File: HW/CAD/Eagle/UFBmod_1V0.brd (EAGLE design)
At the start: 78.1 x 89.8 mm, 63 parts, among them U101 DIGILENT_CMOD_A7, U301 MAX5217, U401 AT86RF215-ZU, U411 ASVTX-13-D-26.000MHZ-I05-T, U511 PE4259, U581 B39871B3440U410, U611 TPS62056DGSR, X599 ANTENNATINY

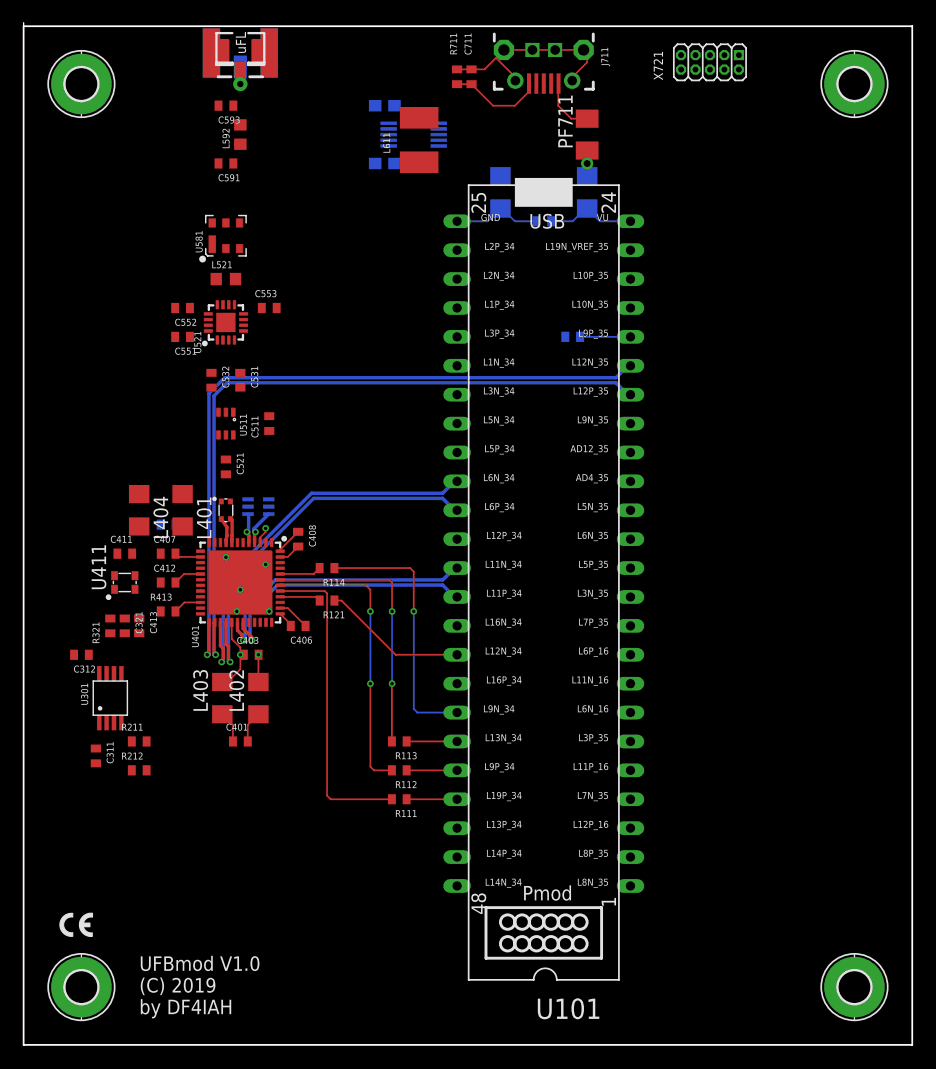
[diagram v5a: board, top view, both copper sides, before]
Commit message: HW_1V0 - CAD/Eagle - connectors added
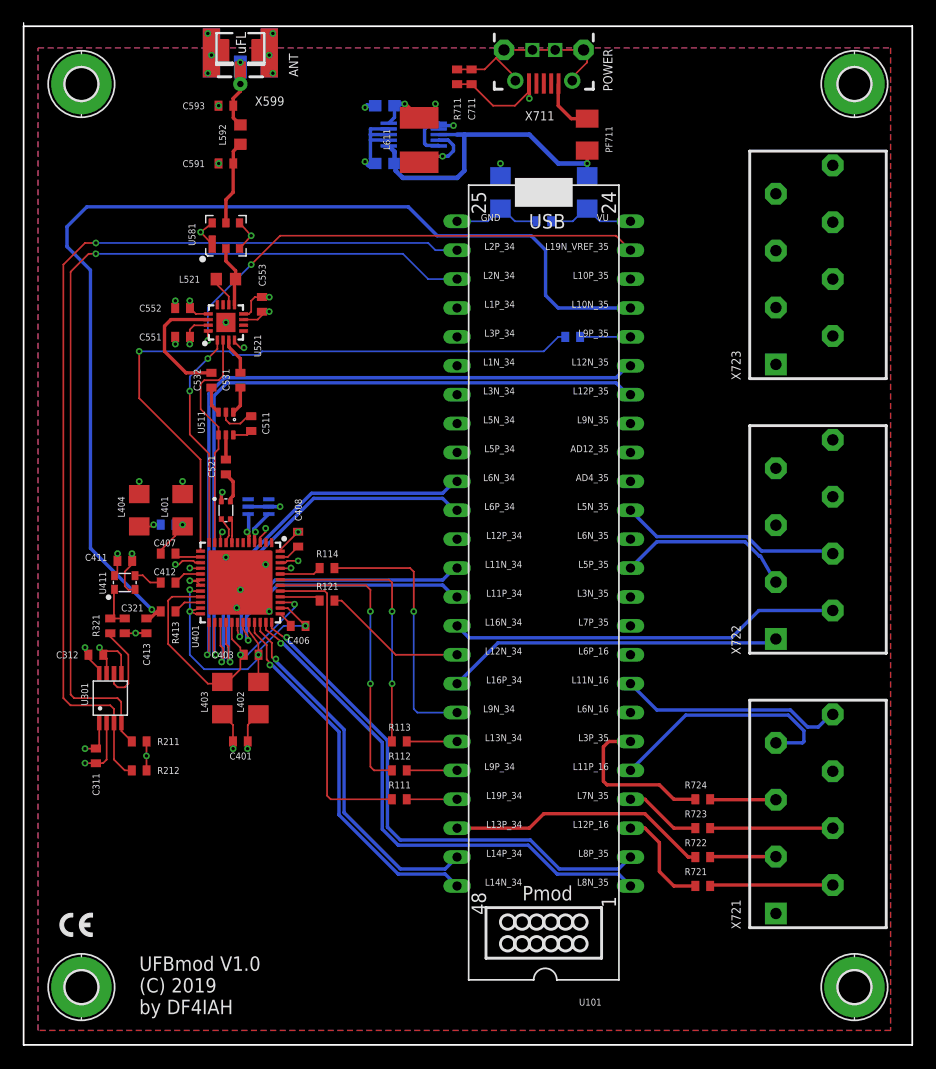
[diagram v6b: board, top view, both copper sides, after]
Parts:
- added R721, R722, R723, R724: 100R, df4iah_rcl:R0402
- added X722, X723: PHOENIX_1990067_1X8X2MM50_PTSA-0-5, df4iah_connector:PHOENIX_1990067_1X8X2MM50_PTSA-0-5
- X721: value (none) -> PHOENIX_1990067_1X8X2MM50_PTSA-0-5; device df4iah_connector:2X05_1MM27 -> df4iah_connector:PHOENIX_1990067_1X8X2MM50_PTSA-0-5
- moved X721 68.2 mm to (71.1, 19.1), turned to 90 degrees
- moved C511 1.59 mm to (20.0, 54.6)
- moved C312 1.27 mm to (6.35, 34.3)
- moved C553 0.71 mm to (21.0, 65.1), turned to 90 degrees
- moved C413 0.63 mm to (10.8, 36.8)
- moved C411 0.63 mm to (8.89, 42.5)
- renumbered J711 to X711
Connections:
- new net FPGA_11_16_N: U101.8, X721.8
- new net FPGA_11_16_P: U101.5, X721.7
- new net FPGA_12P16: R721.1, U101.3
- new net FPGA_12P16_R: R721.2, X721.2
- new net FPGA_13P_34: R722.1, U101.46
- new net FPGA_13P_34_R: R722.2, X721.3
- new net FPGA_16_34_N: U101.39, X722.2
- new net FPGA_16_34_P: U101.41, X722.1
- new net FPGA_3P35: R724.1, U101.6
- new net FPGA_3P35_R: R724.2, X721.5
- new net FPGA_3_34_N: U101.29
- new net FPGA_3_34_P: U101.31
- new net FPGA_5_34_N: U101.32, X722.6
- new net FPGA_5_34_P: U101.33, X722.5
- new net FPGA_5_35_N: U101.14, X722.4
- new net FPGA_5_35_P: U101.12, X722.3
- new net FPGA_7N35: R723.1, U101.4
- new net FPGA_7N35_R: R723.2, X721.4
- net GND: now also X721.1, X721.6
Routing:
- net FPGA_TRX_CLKO: track 0.00 -> 95.0 mm, vias 0 -> 1
- net FPGA_I2C_SCL: track 0.00 -> 85.0 mm, vias 0 -> 1
- net FPGA_I2C_SDA: track 0.00 -> 81.3 mm, vias 0 -> 1
- net GND: track 11.1 -> 72.3 mm, vias 0 -> 29
- net TRX_RSTN: track 0.00 -> 58.0 mm, vias 0 -> 1
- net TRX_RXD24_N: track 0.00 -> 46.7 mm, vias 0 -> 1
- net TRX_RXD24_P: track 0.00 -> 45.9 mm, vias 0 -> 1
- net FE09_MODE: track 0.00 -> 44.0 mm, vias 0 -> 2
- net FPGA_16_34_N: track 0.00 -> 34.4 mm
- net TRX_RXCLK_N: track 0.00 -> 33.3 mm, vias 0 -> 1
- net TRX_RXCLK_P: track 0.00 -> 32.5 mm, vias 0 -> 1
- net +3V3: track 2.78 -> 34.9 mm, vias 0 -> 11
- net FPGA_16_34_P: track 0.00 -> 29.6 mm
- net +5V: track 2.26 -> 28.5 mm
- net TRX_DVSS: track 5.28 -> 29.7 mm, vias 1 -> 4
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- added copper zone on layer 15, net +3V3
- added copper zone on layer 1, net GND
- added copper zone on layer 16, net GND
- added copper zone on layer 2, net GND
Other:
- board text added: "ANT"
- board text added: "POWER"
- board text added: "X599"

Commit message: HW_1V0 - CAD/Eagle - one more line pair added to the connector
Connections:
- net FPGA_3_34_N: now also X722.8
- net FPGA_3_34_P: now also X722.7
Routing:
- net FPGA_3_34_N: track 0.00 -> 36.8 mm
- net FPGA_5_34_N: track 0.00 -> 35.7 mm
- net FPGA_3_34_P: track 0.00 -> 33.3 mm
- net FPGA_5_34_P: track 0.00 -> 32.1 mm
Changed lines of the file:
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@@
 <contactref element="X722" pad="5"/>
 <contactref element="U101" pad="33"/>
-<wire x1="38.1" y1="52.07" x2="66.12" y2="45.68" width="0" layer="19" extent="1-1"/>
+<wire x1="38.1" y1="52.07" x2="38.325" y2="52.07" width="0.3" layer="16"/>
+<wire x1="38.325" y1="52.07" x2="39.37" y2="53.115" width="0.3" layer="16"/>
+<wire x1="39.37" y1="53.115" x2="43.0868" y2="53.115" width="0.3" layer="16"/>
+<wire x1="43.0868" y1="53.115" x2="48.1668" y2="48.035" width="0.3" layer="16"/>
+<wire x1="48.1668" y1="48.035" x2="64.77" y2="48.035" width="0.3" layer="16"/>
+<wire x1="64.77" y1="48.035" x2="66.12" y2="46.685" width="0.3" layer="16"/>
+<wire x1="66.12" y1="46.685" x2="66.12" y2="45.68" width="0.3" layer="16"/>
 </signal>
 <signal name="FPGA_5_34_N" class="1">
 <contactref element="X722" pad="6"/>
 <contactref element="U101" pad="32"/>
-<wire x1="38.1" y1="54.61" x2="71.12" y2="48.18" width="0" layer="19" extent="1-1"/>
+<wire x1="38.1" y1="54.61" x2="38.325" y2="54.61" width="0.3" layer="16"/>
+<wire x1="38.325" y1="54.61" x2="39.37" y2="53.565" width="0.3" layer="16"/>
+<wire x1="39.37" y1="53.565" x2="43.2732" y2="53.565" width="0.3" layer="16"/>
+<wire x1="43.2732" y1="53.565" x2="48.3532" y2="48.485" width="0.3" layer="16"/>
+<wire x1="48.3532" y1="48.485" x2="70.815" y2="48.485" width="0.3" layer="16"/>
+<wire x1="70.815" y1="48.485" x2="71.12" y2="48.18" width="0.3" layer="16"/>
 </signal>
 <signal name="FPGA_3_34_P" class="1">
 <contactref element="U101" pad="31"/>
+<contactref element="X722" pad="7"/>
+<wire x1="38.1" y1="57.15" x2="40.415" y2="59.465" width="0.3" layer="1"/>
+<wire x1="40.415" y1="59.465" x2="44.3568" y2="59.465" width="0.3" layer="1"/>
+<wire x1="44.3568" y1="59.465" x2="50.7068" y2="53.115" width="0.3" layer="1"/>
+<wire x1="50.7068" y1="53.115" x2="64.77" y2="53.115" width="0.3" layer="1"/>
+<wire x1="64.77" y1="53.115" x2="66.12" y2="51.765" width="0.3" layer="1"/>
+<wire x1="66.12" y1="51.765" x2="66.12" y2="50.68" width="0.3" layer="1"/>
 </signal>
 <signal name="FPGA_3_34_N" class="1">
 <contactref element="U101" pad="29"/>
+<contactref element="X722" pad="8"/>
+<wire x1="38.1" y1="62.23" x2="40.415" y2="59.915" width="0.3" layer="1"/>
+<wire x1="40.415" y1="59.915" x2="44.5432" y2="59.915" width="0.3" layer="1"/>
+<wire x1="44.5432" y1="59.915" x2="50.8932" y2="53.565" width="0.3" layer="1"/>
+<wire x1="50.8932" y1="53.565" x2="70.735" y2="53.565" width="0.3" layer="1"/>
+<wire x1="70.735" y1="53.565" x2="71.12" y2="53.18" width="0.3" layer="1"/>
 </signal>
 </signals>

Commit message: HW_1V0 - V1.0 at the board house
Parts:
- added C221, C222: 1nF, df4iah_rcl:C0402
- added C595, C597: 0pF, df4iah_rcl:C0402
- added D141: ASMT-YTB7-0AA02_RGB, df4iah_led:ASMT-YTB7_0AA02_RGB
- added FIDU_BL, FIDU_BR, FIDU_TL, FIDU_TR: (no value), df4iah_fiducial:FIDUCIAL_MARK_1MM
- added L596: 0nH, df4iah_rcl:L0603
- added R141: 180R, df4iah_rcl:R0402
- added R142, R143: 130R, df4iah_rcl:R0402
- added R151, R152, R521: 1kR, df4iah_rcl:R0402
- added R733, R734, R735, R736: 100R, df4iah_rcl:R0402
- added X221: TTE_EN11-HSM, df4iah_switch:TTE_EN11-HSM
- added X595: ANTENNATINY, _c2h:SMA_UFL_PAD_TINY
- U521: value (none) -> RFX1010
- X711: value (none) -> MOLEX 105017-0001
- renumbered X599 to X591
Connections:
- net ANT renamed ANT09
- net ANT_MATCH renamed ANT09_MATCH
- new net ANT24: C597.1, L596.2, X595.ANT1, X595.ANT2, X595.ANT3
- new net FPGA_10P35: R736.1, U101.22
- new net FPGA_10P35_R: R736.2, X723.6
- new net FPGA_12P34: R735.1, U101.36
- new net FPGA_12P34_R: R735.2, X723.5
- new net FPGA_1_34_N: U101.30, X723.2
- new net FPGA_1_34_P: U101.28, X723.1
- new net FPGA_9N35: R734.1, U101.17
- new net FPGA_9N35_R: R734.2, X723.4
- new net FPGA_AD12: R733.1, U101.16
- new net FPGA_AD12_R: R733.2, X723.3
- new net LED_B: D141.6, R143.1
- new net LED_B_R: R143.2, U101.11
- new net LED_G: D141.5, R142.1
- new net LED_G_R: R142.2, U101.10
- new net LED_R: D141.4, R141.1
- new net LED_R_R: R141.2, U101.9
- new net ROT_I: R151.2, U101.7
- new net ROT_I_R: C221.1, R151.1, X221.A
- new net ROT_Q: R152.2, U101.13
- new net ROT_Q_R: C222.1, R152.1, X221.B
- net +3V3: now also X721.6
- net +5V: now also X723.7
- net FE09_DET: now also R521.1
- net FPGA_FE09_DET: now also R521.2
- net GND: now also C221.2, C222.2, C595.2, C597.2, D141.1, D141.2, D141.3, X221.C, X221.D, X595.GND1, X595.GND2, X595.GND3, X595.GND4, X723.8; no longer U611.2, U611.4, X721.6
- net TRX_RF24: now also C595.1, L596.1
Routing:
- net FPGA_12P34: track 0.00 -> 62.8 mm
- net FPGA_1_34_N: track 0.00 -> 52.4 mm
- net FE09_DET: track 0.00 -> 51.5 mm, vias 0 -> 1
- net FPGA_1_34_P: track 0.00 -> 50.8 mm
- net ROT_Q_R: track 0.00 -> 49.8 mm, vias 0 -> 1
- net ROT_I_R: track 0.00 -> 39.6 mm, vias 0 -> 1
- net TRX_RF24: track 0.00 -> 34.3 mm, vias 0 -> 1
- net +5V: track 28.5 -> 46.3 mm
- net FPGA_9N35: track 0.00 -> 16.2 mm, vias 0 -> 1
- net FPGA_AD12: track 0.00 -> 16.2 mm, vias 0 -> 1
- net GND: track 72.3 -> 88.2 mm, vias 29 -> 40
- net FPGA_10P35_R: track 0.00 -> 10.8 mm
- net FPGA_9N35_R: track 0.00 -> 10.8 mm
- net LED_B: track 0.00 -> 9.98 mm
- net FPGA_10P35: track 0.00 -> 9.29 mm
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- added copper zone on layer 2, net TRX_AVSS
- added copper zone on layer 15, net TRX_EVDD
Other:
- board size 78.1 x 89.8 mm -> 78.1 x 89.5 mm
- board text added: "ANT09"
- board text added: "ANT24"
- board text added: "BOT"
- board text added: "L2"
- board text added: "L3"
- board text added: "TOP"
- board text added: "X591"
- board text added: "X595"
- board text removed: "ANT"
- board text removed: "X599"
